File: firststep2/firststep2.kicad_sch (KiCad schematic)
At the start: 2 parts, among them J1 Analog, J2 Digital

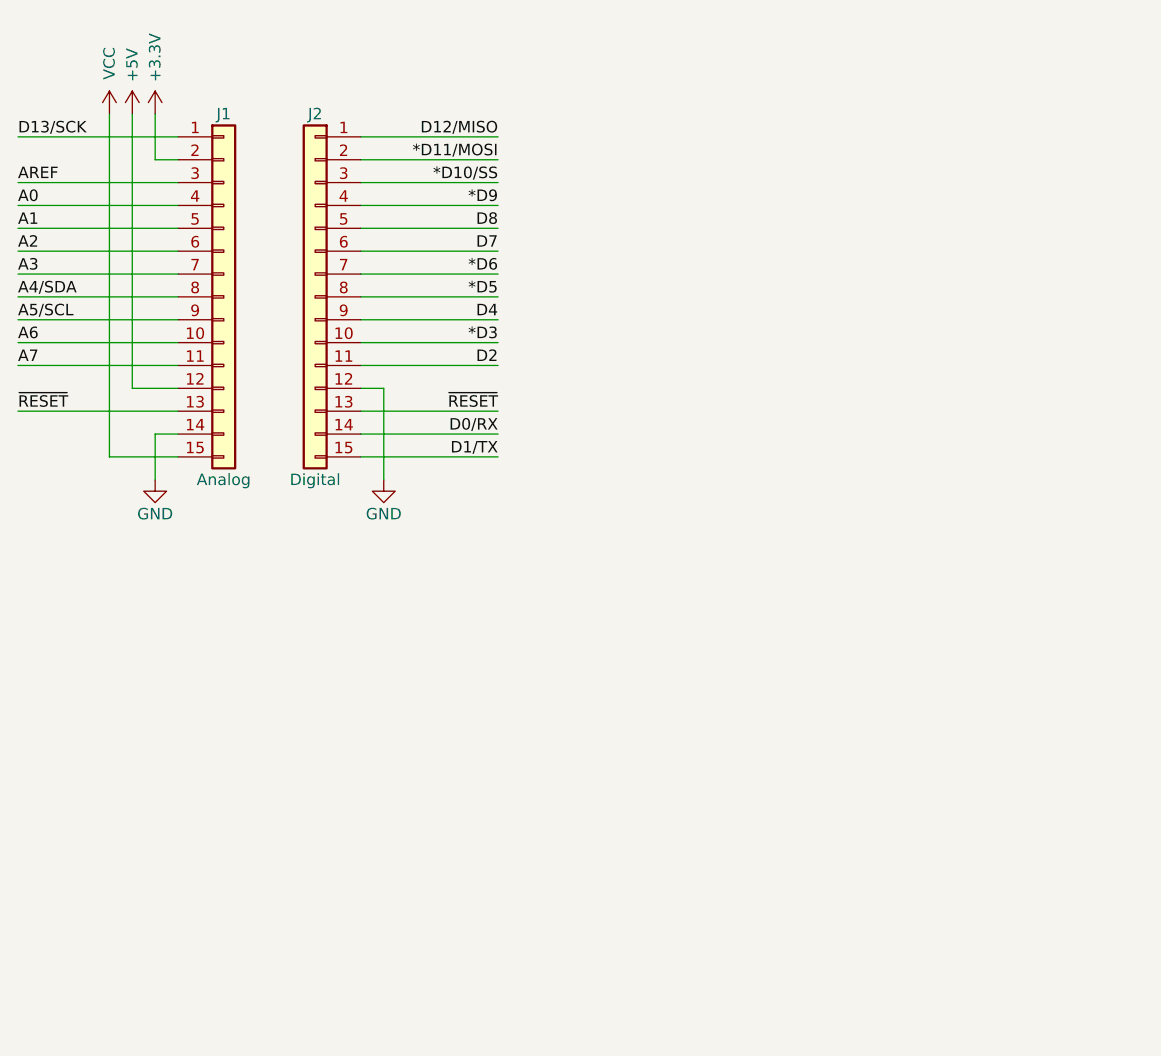
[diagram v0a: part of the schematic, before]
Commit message: added atmega_logic, changed lm to tl
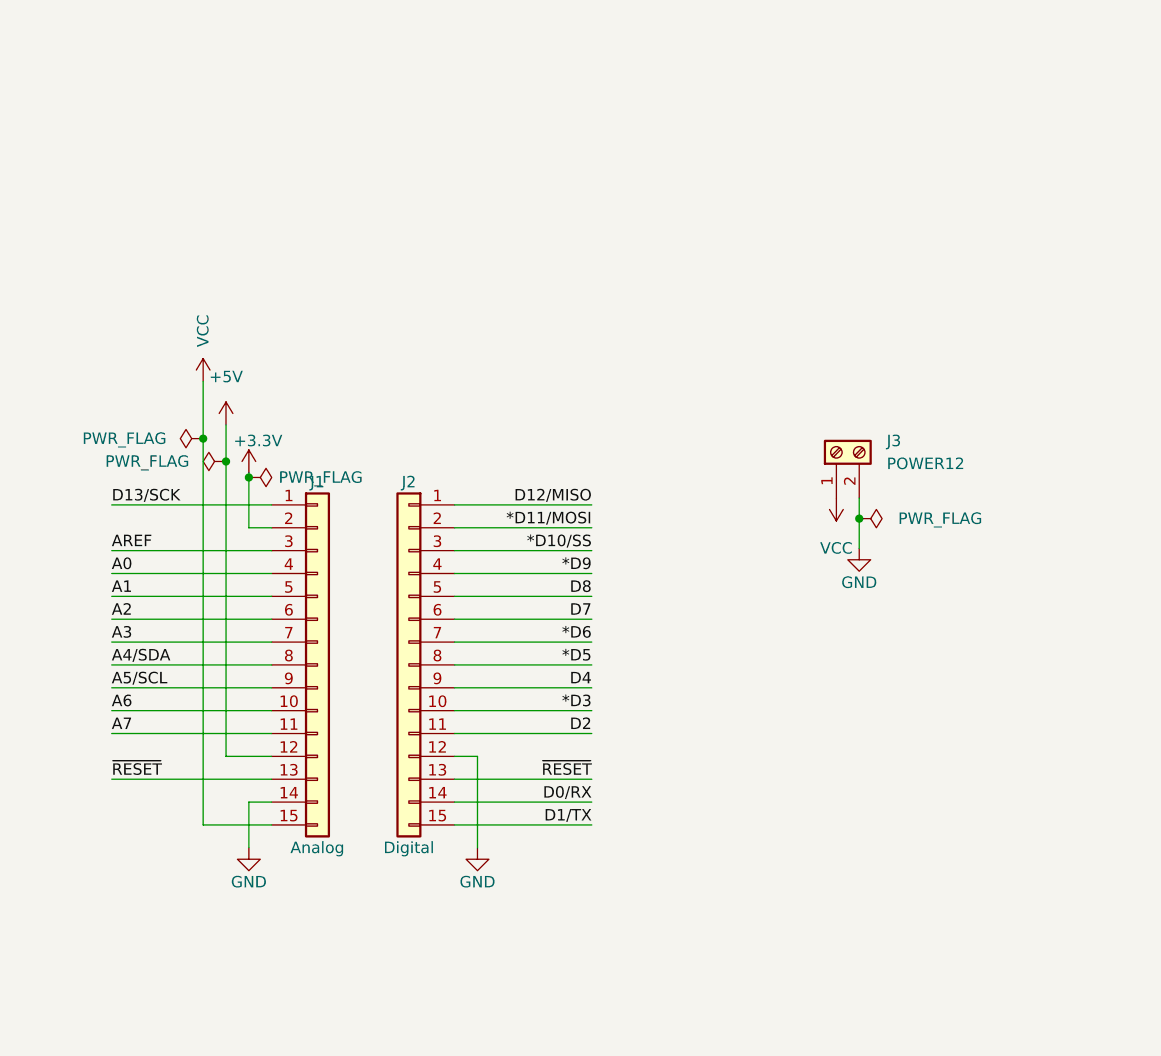
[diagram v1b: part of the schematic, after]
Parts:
- added J3: POWER12, Connector_PinHeader_2.54mm:PinHeader_1x01_P2.54mm_Vertical, symbol Connector:Screw_Terminal_01x02
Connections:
- net GND: now also J3.2 (Pin_2)
- net VCC: now also J3.1 (Pin_1)
- net +3V3 renamed +3.3V
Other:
- moved on the sheet: J1, J2

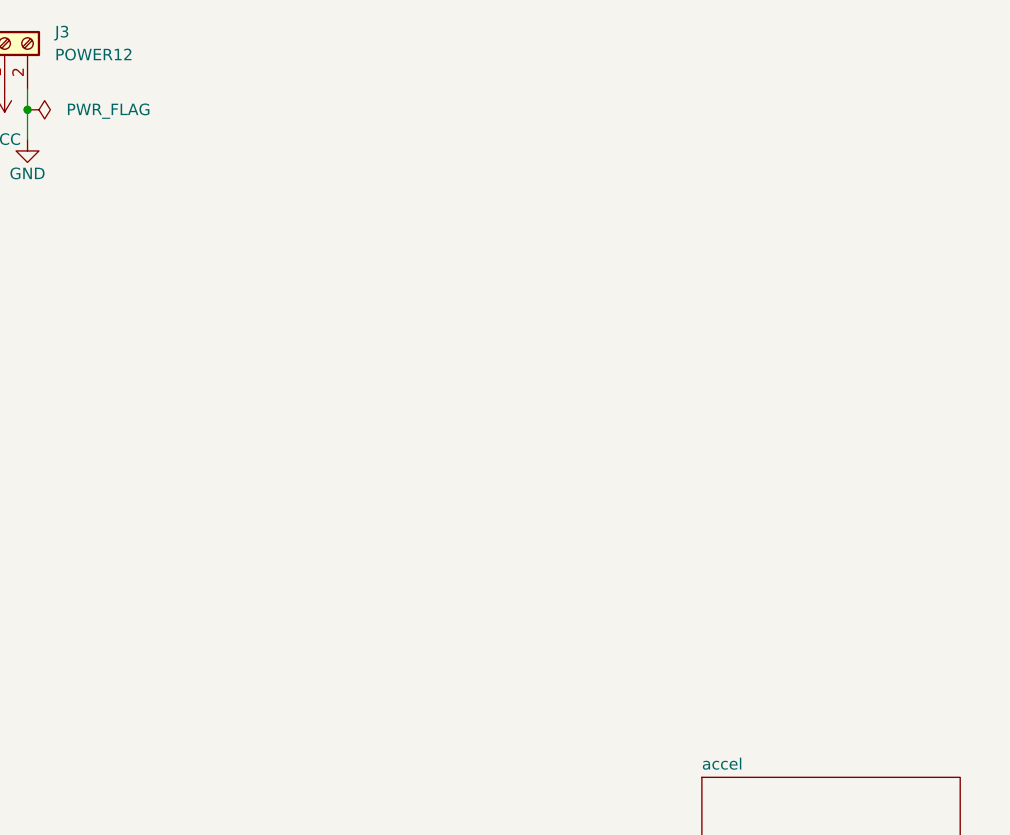
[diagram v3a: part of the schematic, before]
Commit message: added NE555 50kHz gen
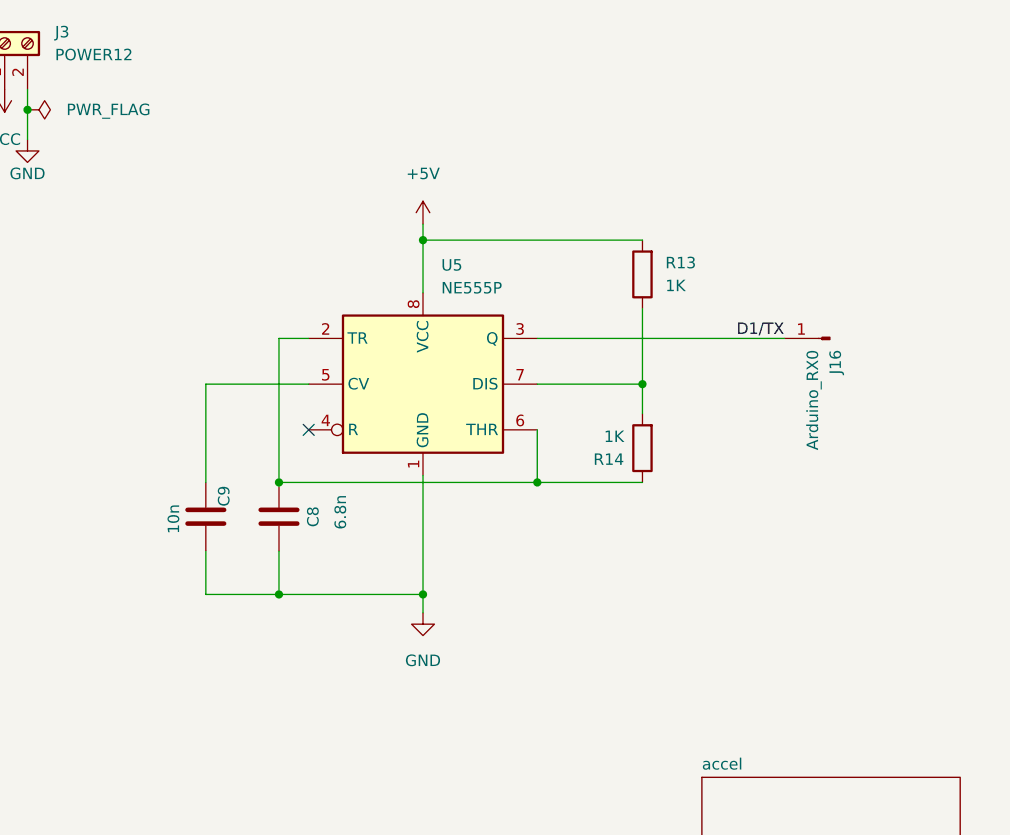
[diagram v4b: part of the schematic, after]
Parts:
- added C8: 6.8n, Capacitor_THT:C_Disc_D3.0mm_W2.0mm_P2.50mm, symbol Device:C
- added C9: 10n, Capacitor_THT:C_Disc_D3.0mm_W2.0mm_P2.50mm, symbol Device:C
- added J16: Arduino_RX0, Connector_PinHeader_2.54mm:PinHeader_1x01_P2.54mm_Vertical, symbol Connector:Conn_01x01_Male
- added R13, R14: 1K, Resistor_THT:R_Axial_DIN0207_L6.3mm_D2.5mm_P7.62mm_Horizontal, symbol Device:R
- added U5: NE555P, Package_DIP:DIP-8_W7.62mm, symbol Timer:NE555P
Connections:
- net +5V: now also R13.2, U5.8 (VCC)
- net D1/TX: now also J16.1 (Pin_1), U5.3 (Q)
- net GND: now also C8.1, C9.1, U5.1 (GND)
- new net: C8.2, R14.1, U5.2 (TR), U5.6 (THR)
- new net: R13.1, R14.2, U5.7 (DIS)
- new net: C9.2, U5.5 (CV)
- no-connect marks 0 -> 1
